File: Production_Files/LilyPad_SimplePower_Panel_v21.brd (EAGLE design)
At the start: 28.4 x 28.4 mm, 20 parts, among them U1 MCP73831

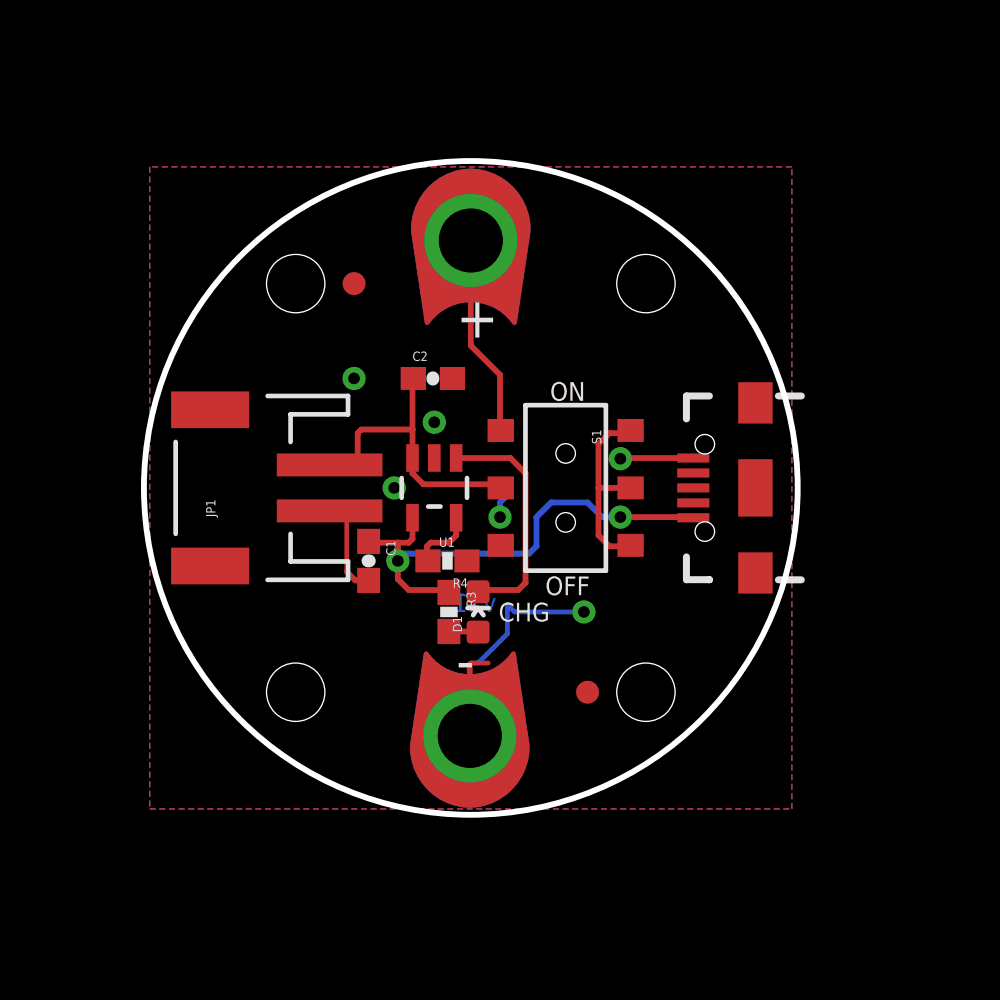
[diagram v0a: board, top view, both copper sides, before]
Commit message: Rotating board 45 degrees for panelization
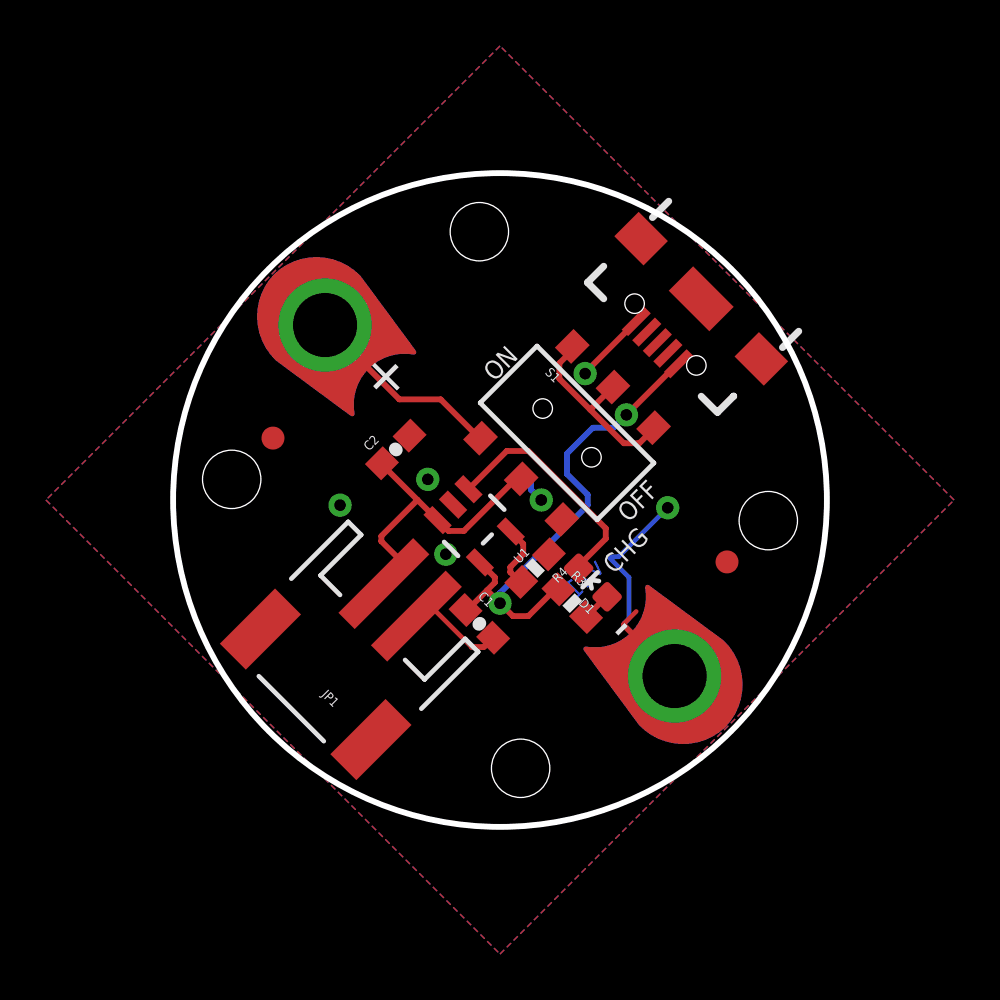
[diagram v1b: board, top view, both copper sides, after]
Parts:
- moved STANDOFF4 10.3 mm to (2.17, -14.7), turned to 45 degrees
- moved JP3 9.31 mm to (8.89, -10.7), turned to 135 degrees
- moved STANDOFF3 9.17 mm to (12.9, -3.96), turned to 45 degrees
- moved STANDOFF1 8.96 mm to (-10.4, -2.17), turned to 45 degrees
- moved JP4 8.56 mm to (10.0, 5.69), turned to 225 degrees
- moved JP1 8.56 mm to (-5.69, -10.0), turned to 135 degrees
- moved FID2 8.30 mm to (11.1, -5.76), turned to 45 degrees
- moved STANDOFF2 7.59 mm to (0.37, 8.61), turned to 45 degrees
- moved FID1 7.59 mm to (-8.61, -0.37), turned to 45 degrees
- moved JP2 7.35 mm to (-6.36, 4.57), turned to 315 degrees
- moved C1 5.54 mm to (0.37, -8.45), turned to 315 degrees
- moved R3 5.38 mm to (4.41, -7.56), turned to 315 degrees
- moved D1 5.15 mm to (5.31, -6.66), turned to 45 degrees
- moved R4 3.83 mm to (2.80, -6.03), turned to 225 degrees
- moved JP5 3.54 mm to (2.39, -5.76), turned to 315 degrees
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
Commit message: Created panel v21
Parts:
- added C10, C11, C12, C13, C14, C15, C16, C17, C18, C19, C20, C21, C22, C23, C24, C25, C26, C27, C28, C29, C3, C30, C31, C32, C33, C34, C35, C36, C37, C38, C39, C4, C40, C41, C42, C43, C44, C45, C46, C47, C48, C49, C5, C50, C51, C52, C53, C54, C55, C56, C57, C58, C59, C6, C60, C61, C62, C63, C64, C7, C8, C9: 4.7uF, SparkFun-Capacitors:0603-CAP
- added D10, D11, D12, D13, D14, D15, D16, D17, D18, D19, D2, D20, D21, D22, D23, D24, D25, D26, D27, D28, D29, D3, D30, D31, D32, D4, D5, D6, D7, D8, D9: Yellow, SparkFun-LED:LED-0603
- added E$1, E$6: (no value), SparkFun-Retired:FIDUCIAL-1.5X3
- added E$2, E$3, E$4, E$5: (no value), SparkFun-Aesthetics:FIDUCIAL-1X2
- added FID10, FID11, FID12, FID13, FID14, FID15, FID16, FID17, FID18, FID19, FID20, FID21, FID22, FID23, FID24, FID25, FID26, FID27, FID28, FID29, FID3, FID30, FID31, FID32, FID33, FID34, FID35, FID36, FID37, FID38, FID39, FID4, FID40, FID41, FID42, FID43, FID44, FID45, FID46, FID47, FID48, FID49, FID5, FID50, FID51, FID52, FID53, FID54, FID55, FID56, FID57, FID58, FID59, FID6, FID60, FID61, FID62, FID63, FID64, FID7, FID8, FID9: FIDUCIAL1X2, SparkFun-Aesthetics:FIDUCIAL-1X2
- added JP10, JP100, JP105, JP110, JP115, JP120, JP125, JP130, JP135, JP140, JP145, JP15, JP150, JP155, JP160, JP20, JP25, JP30, JP35, JP40, JP45, JP50, JP55, JP60, JP65, JP70, JP75, JP80, JP85, JP90, JP95: USB_MICROB_PLUGCONN-11752, SparkFun-Connectors:USB-B-MICRO-SMD_V03
- added JP101, JP106, JP11, JP111, JP116, JP121, JP126, JP131, JP136, JP141, JP146, JP151, JP156, JP16, JP21, JP26, JP31, JP36, JP41, JP46, JP51, JP56, JP6, JP61, JP66, JP71, JP76, JP81, JP86, JP91, JP96: M02-JST-2MM-SMT, SparkFun-Connectors:JST-2-SMD
- added JP102, JP103, JP107, JP108, JP112, JP113, JP117, JP118, JP12, JP122, JP123, JP127, JP128, JP13, JP132, JP133, JP137, JP138, JP142, JP143, JP147, JP148, JP152, JP153, JP157, JP158, JP17, JP18, JP22, JP23, JP27, JP28, JP32, JP33, JP37, JP38, JP42, JP43, JP47, JP48, JP52, JP53, JP57, JP58, JP62, JP63, JP67, JP68, JP7, JP72, JP73, JP77, JP78, JP8, JP82, JP83, JP87, JP88, JP92, JP93, JP97, JP98: SEWTAP9, LilyPad-Wearables:PETAL-LONG-1-2SIDE
- added JP104, JP109, JP114, JP119, JP124, JP129, JP134, JP139, JP14, JP144, JP149, JP154, JP159, JP19, JP24, JP29, JP34, JP39, JP44, JP49, JP54, JP59, JP64, JP69, JP74, JP79, JP84, JP89, JP9, JP94, JP99: SFE_LOGO_FLAME.1_INCH, SparkFun-Aesthetics:SFE_LOGO_FLAME_.1
- added R1, R11, R13, R15, R17, R19, R21, R23, R25, R27, R29, R31, R33, R35, R37, R39, R41, R43, R45, R47, R49, R5, R51, R53, R55, R57, R59, R61, R63, R7, R9: 330, SparkFun-Resistors:0603-RES
- added R10, R12, R14, R16, R18, R2, R20, R22, R24, R26, R28, R30, R32, R34, R36, R38, R40, R42, R44, R46, R48, R50, R52, R54, R56, R58, R6, R60, R62, R64, R8: 2.0k, SparkFun-Resistors:0603-RES
- added S10, S11, S12, S13, S14, S15, S16, S17, S18, S19, S2, S20, S21, S22, S23, S24, S25, S26, S27, S28, S29, S3, S30, S31, S32, S4, S5, S6, S7, S8, S9: DPDT, SparkFun-Electromechanical:AYZ0202
- added STANDOFF10, STANDOFF100, STANDOFF101, STANDOFF102, STANDOFF103, STANDOFF104, STANDOFF105, STANDOFF106, STANDOFF107, STANDOFF108, STANDOFF109, STANDOFF11, STANDOFF110, STANDOFF111, STANDOFF112, STANDOFF113, STANDOFF114, STANDOFF115, STANDOFF116, STANDOFF117, STANDOFF118, STANDOFF119, STANDOFF12, STANDOFF120, STANDOFF121, STANDOFF122, STANDOFF123, STANDOFF124, STANDOFF125, STANDOFF126, STANDOFF127, STANDOFF128, STANDOFF13, STANDOFF14, STANDOFF15, STANDOFF16, STANDOFF17, STANDOFF18, STANDOFF19, STANDOFF20, STANDOFF21, STANDOFF22, STANDOFF23, STANDOFF24, STANDOFF25, STANDOFF26, STANDOFF27, STANDOFF28, STANDOFF29, STANDOFF30, STANDOFF31, STANDOFF32, STANDOFF33, STANDOFF34, STANDOFF35, STANDOFF36, STANDOFF37, STANDOFF38, STANDOFF39, STANDOFF40, STANDOFF41, STANDOFF42, STANDOFF43, STANDOFF44, STANDOFF45, STANDOFF46, STANDOFF47, STANDOFF48, STANDOFF49, STANDOFF5, STANDOFF50, STANDOFF51, STANDOFF52, STANDOFF53, STANDOFF54, STANDOFF55, STANDOFF56, STANDOFF57, STANDOFF58, STANDOFF59, STANDOFF6, STANDOFF60, STANDOFF61, STANDOFF62, STANDOFF63, STANDOFF64, STANDOFF65, STANDOFF66, STANDOFF67, STANDOFF68, STANDOFF69, STANDOFF7, STANDOFF70, STANDOFF71, STANDOFF72, STANDOFF73, STANDOFF74, STANDOFF75, STANDOFF76, STANDOFF77, STANDOFF78, STANDOFF79, STANDOFF8, STANDOFF80, STANDOFF81, STANDOFF82, STANDOFF83, STANDOFF84, STANDOFF85, STANDOFF86, STANDOFF87, STANDOFF88, STANDOFF89, STANDOFF9, STANDOFF90, STANDOFF91, STANDOFF92, STANDOFF93, STANDOFF94, STANDOFF95, STANDOFF96, STANDOFF97, STANDOFF98, STANDOFF99: SEW-HOLE-NO-PAD, Local Library:SEW-HOLE-NO-PAD
- added U$10, U$12, U$14, U$16, U$18, U$20, U$22, U$24, U$26, U$28, U$3, U$30, U$32, U$34, U$36, U$38, U$40, U$42, U$44, U$46, U$48, U$50, U$52, U$54, U$56, U$58, U$6, U$60, U$62, U$64, U$8: LOGO-LPLP, LilyPad-Wearables:LOGO-LILYPAD
- added U$11, U$13, U$15, U$17, U$19, U$2, U$21, U$23, U$25, U$27, U$29, U$31, U$33, U$35, U$37, U$39, U$4, U$41, U$43, U$45, U$47, U$49, U$51, U$53, U$55, U$57, U$59, U$61, U$63, U$7, U$9: OSHW-LOGOS, SparkFun-Aesthetics:OSHW-LOGO-S
- added U10, U11, U12, U13, U14, U15, U16, U17, U18, U19, U2, U20, U21, U22, U23, U24, U25, U26, U27, U28, U29, U3, U30, U31, U32, U4, U5, U6, U7, U8, U9: MCP73831, SparkFun-PowerIC:SOT23-5
- moved FID2 35.1 mm to (34.0, 20.9)
- moved C1 35.1 mm to (23.2, 18.2)
- moved C2 35.1 mm to (19.6, 25.8)
- moved D1 35.1 mm to (28.2, 20.0)
- moved FID1 35.1 mm to (14.3, 26.3)
- moved JP1 35.1 mm to (17.2, 16.6)
- moved JP2 35.1 mm to (16.5, 31.2)
- moved JP3 35.1 mm to (31.7, 15.9)
- moved JP4 35.1 mm to (32.9, 32.4)
- moved JP5 35.1 mm to (25.3, 20.9)
- moved R3 35.1 mm to (27.3, 19.1)
- moved R4 35.1 mm to (25.7, 20.6)
- moved S1 35.1 mm to (27.0, 26.5)
- moved STANDOFF1 35.1 mm to (12.5, 24.5)
- moved STANDOFF2 35.1 mm to (23.2, 35.3)
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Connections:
- new net GND1: C3.2, C4.2, JP10.GND1, JP6.1, JP7.1, R2.1, U2.2
- new net GND10: C21.2, C22.2, JP51.1, JP52.1, JP55.GND1, R22.1, U11.2
- new net GND11: C23.2, C24.2, JP56.1, JP57.1, JP60.GND1, R24.1, U12.2
- new net GND12: C25.2, C26.2, JP61.1, JP62.1, JP65.GND1, R26.1, U13.2
- new net GND13: C27.2, C28.2, JP66.1, JP67.1, JP70.GND1, R28.1, U14.2
- new net GND14: C29.2, C30.2, JP71.1, JP72.1, JP75.GND1, R30.1, U15.2
- new net GND15: C31.2, C32.2, JP76.1, JP77.1, JP80.GND1, R32.1, U16.2
- new net GND16: C33.2, C34.2, JP81.1, JP82.1, JP85.GND1, R34.1, U17.2
- new net GND17: C35.2, C36.2, JP86.1, JP87.1, JP90.GND1, R36.1, U18.2
- new net GND18: C37.2, C38.2, JP91.1, JP92.1, JP95.GND1, R38.1, U19.2
- new net GND19: C39.2, C40.2, JP100.GND1, JP96.1, JP97.1, R40.1, U20.2
- new net GND2: C5.2, C6.2, JP11.1, JP12.1, JP15.GND1, R6.1, U3.2
- new net GND20: C41.2, C42.2, JP101.1, JP102.1, JP105.GND1, R42.1, U21.2
- new net GND21: C43.2, C44.2, JP106.1, JP107.1, JP110.GND1, R44.1, U22.2
- new net GND22: C45.2, C46.2, JP111.1, JP112.1, JP115.GND1, R46.1, U23.2
- new net GND23: C47.2, C48.2, JP116.1, JP117.1, JP120.GND1, R48.1, U24.2
- new net GND24: C49.2, C50.2, JP121.1, JP122.1, JP125.GND1, R50.1, U25.2
- new net GND25: C51.2, C52.2, JP126.1, JP127.1, JP130.GND1, R52.1, U26.2
- new net GND26: C53.2, C54.2, JP131.1, JP132.1, JP135.GND1, R54.1, U27.2
- new net GND27: C55.2, C56.2, JP136.1, JP137.1, JP140.GND1, R56.1, U28.2
- new net GND28: C57.2, C58.2, JP141.1, JP142.1, JP145.GND1, R58.1, U29.2
- new net GND29: C59.2, C60.2, JP146.1, JP147.1, JP150.GND1, R60.1, U30.2
- new net GND3: C7.2, C8.2, JP16.1, JP17.1, JP20.GND1, R8.1, U4.2
- new net GND30: C61.2, C62.2, JP151.1, JP152.1, JP155.GND1, R62.1, U31.2
- new net GND31: C63.2, C64.2, JP156.1, JP157.1, JP160.GND1, R64.1, U32.2
- new net GND4: C10.2, C9.2, JP21.1, JP22.1, JP25.GND1, R10.1, U5.2
- new net GND5: C11.2, C12.2, JP26.1, JP27.1, JP30.GND1, R12.1, U6.2
- new net GND6: C13.2, C14.2, JP31.1, JP32.1, JP35.GND1, R14.1, U7.2
- new net GND7: C15.2, C16.2, JP36.1, JP37.1, JP40.GND1, R16.1, U8.2
- new net GND8: C17.2, C18.2, JP41.1, JP42.1, JP45.GND1, R18.1, U9.2
- new net GND9: C19.2, C20.2, JP46.1, JP47.1, JP50.GND1, R20.1, U10.2
- new net N$10: R2.2, U2.5
- new net N$100: R40.2, U20.5
- new net N$101: C42.1, JP101.2, S21.5, U21.3
- new net N$102: C41.1, JP105.VBUS1, R41.1, U21.4
- new net N$103: D21.C, U21.1
- new net N$104: D21.A, R41.2
- new net N$105: R42.2, U21.5
- new net N$106: C44.1, JP106.2, S22.5, U22.3
- new net N$107: C43.1, JP110.VBUS1, R43.1, U22.4
- new net N$108: D22.C, U22.1
- new net N$109: D22.A, R43.2
- new net N$11: C6.1, JP11.2, S3.5, U3.3
- new net N$110: R44.2, U22.5
- new net N$111: C46.1, JP111.2, S23.5, U23.3
- new net N$112: C45.1, JP115.VBUS1, R45.1, U23.4
- new net N$113: D23.C, U23.1
- new net N$114: D23.A, R45.2
- new net N$115: R46.2, U23.5
- new net N$116: C48.1, JP116.2, S24.5, U24.3
- new net N$117: C47.1, JP120.VBUS1, R47.1, U24.4
- new net N$118: D24.C, U24.1
- new net N$119: D24.A, R47.2
- new net N$12: C5.1, JP15.VBUS1, R5.1, U3.4
- new net N$120: R48.2, U24.5
- new net N$121: C50.1, JP121.2, S25.5, U25.3
- new net N$122: C49.1, JP125.VBUS1, R49.1, U25.4
- new net N$123: D25.C, U25.1
- new net N$124: D25.A, R49.2
- new net N$125: R50.2, U25.5
- new net N$126: C52.1, JP126.2, S26.5, U26.3
- new net N$127: C51.1, JP130.VBUS1, R51.1, U26.4
- new net N$128: D26.C, U26.1
- new net N$129: D26.A, R51.2
- new net N$13: D3.C, U3.1
- new net N$130: R52.2, U26.5
- new net N$131: C54.1, JP131.2, S27.5, U27.3
- new net N$132: C53.1, JP135.VBUS1, R53.1, U27.4
- new net N$133: D27.C, U27.1
- new net N$134: D27.A, R53.2
- new net N$135: R54.2, U27.5
- new net N$136: C56.1, JP136.2, S28.5, U28.3
- new net N$137: C55.1, JP140.VBUS1, R55.1, U28.4
- new net N$138: D28.C, U28.1
- new net N$139: D28.A, R55.2
- new net N$14: D3.A, R5.2
- new net N$140: R56.2, U28.5
- new net N$141: C58.1, JP141.2, S29.5, U29.3
- new net N$142: C57.1, JP145.VBUS1, R57.1, U29.4
- new net N$143: D29.C, U29.1
- new net N$144: D29.A, R57.2
- new net N$145: R58.2, U29.5
- new net N$146: C60.1, JP146.2, S30.5, U30.3
- new net N$147: C59.1, JP150.VBUS1, R59.1, U30.4
- new net N$148: D30.C, U30.1
- new net N$149: D30.A, R59.2
- new net N$15: R6.2, U3.5
- new net N$150: R60.2, U30.5
- new net N$151: C62.1, JP151.2, S31.5, U31.3
- new net N$152: C61.1, JP155.VBUS1, R61.1, U31.4
- new net N$153: D31.C, U31.1
- new net N$154: D31.A, R61.2
- new net N$155: R62.2, U31.5
- new net N$156: C64.1, JP156.2, S32.5, U32.3
- new net N$157: C63.1, JP160.VBUS1, R63.1, U32.4
- new net N$158: D32.C, U32.1
- new net N$159: D32.A, R63.2
- new net N$16: C8.1, JP16.2, S4.5, U4.3
- new net N$160: R64.2, U32.5
- new net N$17: C7.1, JP20.VBUS1, R7.1, U4.4
- new net N$18: D4.C, U4.1
- new net N$19: D4.A, R7.2
- new net N$2: C4.1, JP6.2, S2.5, U2.3
- new net N$20: R8.2, U4.5
- new net N$21: C10.1, JP21.2, S5.5, U5.3
- new net N$22: C9.1, JP25.VBUS1, R9.1, U5.4
- new net N$23: D5.C, U5.1
- new net N$24: D5.A, R9.2
- new net N$25: R10.2, U5.5
- new net N$26: C12.1, JP26.2, S6.5, U6.3
- new net N$27: C11.1, JP30.VBUS1, R11.1, U6.4
- new net N$28: D6.C, U6.1
- new net N$29: D6.A, R11.2
- new net N$30: R12.2, U6.5
- new net N$31: C14.1, JP31.2, S7.5, U7.3
- new net N$32: C13.1, JP35.VBUS1, R13.1, U7.4
- new net N$33: D7.C, U7.1
- new net N$34: D7.A, R13.2
- new net N$35: R14.2, U7.5
- new net N$36: C16.1, JP36.2, S8.5, U8.3
- new net N$37: C15.1, JP40.VBUS1, R15.1, U8.4
- new net N$38: D8.C, U8.1
- new net N$39: D8.A, R15.2
- new net N$40: R16.2, U8.5
- new net N$41: C18.1, JP41.2, S9.5, U9.3
- new net N$42: C17.1, JP45.VBUS1, R17.1, U9.4
- new net N$43: D9.C, U9.1
- new net N$44: D9.A, R17.2
- new net N$45: R18.2, U9.5
- new net N$46: C20.1, JP46.2, S10.5, U10.3
- new net N$47: C19.1, JP50.VBUS1, R19.1, U10.4
- new net N$48: D10.C, U10.1
- new net N$49: D10.A, R19.2
- new net N$50: R20.2, U10.5
- new net N$51: C22.1, JP51.2, S11.5, U11.3
- new net N$52: C21.1, JP55.VBUS1, R21.1, U11.4
- new net N$53: D11.C, U11.1
- new net N$54: D11.A, R21.2
- new net N$55: R22.2, U11.5
- new net N$56: C24.1, JP56.2, S12.5, U12.3
- new net N$57: C23.1, JP60.VBUS1, R23.1, U12.4
- new net N$58: D12.C, U12.1
- new net N$59: D12.A, R23.2
- new net N$6: C3.1, JP10.VBUS1, R1.1, U2.4
- new net N$60: R24.2, U12.5
- new net N$61: C26.1, JP61.2, S13.5, U13.3
- new net N$62: C25.1, JP65.VBUS1, R25.1, U13.4
- new net N$63: D13.C, U13.1
- new net N$64: D13.A, R25.2
- new net N$65: R26.2, U13.5
- new net N$66: C28.1, JP66.2, S14.5, U14.3
- new net N$67: C27.1, JP70.VBUS1, R27.1, U14.4
- new net N$68: D14.C, U14.1
- new net N$69: D14.A, R27.2
- new net N$70: R28.2, U14.5
- new net N$71: C30.1, JP71.2, S15.5, U15.3
- new net N$72: C29.1, JP75.VBUS1, R29.1, U15.4
- new net N$73: D15.C, U15.1
- new net N$74: D15.A, R29.2
- new net N$75: R30.2, U15.5
- new net N$76: C32.1, JP76.2, S16.5, U16.3
- new net N$77: C31.1, JP80.VBUS1, R31.1, U16.4
- new net N$78: D16.C, U16.1
- new net N$79: D16.A, R31.2
- new net N$8: D2.C, U2.1
- new net N$80: R32.2, U16.5
- new net N$81: C34.1, JP81.2, S17.5, U17.3
- new net N$82: C33.1, JP85.VBUS1, R33.1, U17.4
- new net N$83: D17.C, U17.1
- new net N$84: D17.A, R33.2
- new net N$85: R34.2, U17.5
- new net N$86: C36.1, JP86.2, S18.5, U18.3
- new net N$87: C35.1, JP90.VBUS1, R35.1, U18.4
- new net N$88: D18.C, U18.1
- new net N$89: D18.A, R35.2
- new net N$9: D2.A, R1.2
- new net N$90: R36.2, U18.5
- new net N$91: C38.1, JP91.2, S19.5, U19.3
- new net N$92: C37.1, JP95.VBUS1, R37.1, U19.4
- new net N$93: D19.C, U19.1
- new net N$94: D19.A, R37.2
- new net N$95: R38.2, U19.5
- new net N$96: C40.1, JP96.2, S20.5, U20.3
- new net N$97: C39.1, JP100.VBUS1, R39.1, U20.4
- new net N$98: D20.C, U20.1
- new net N$99: D20.A, R39.2
- new net SINK10: S10.1, S10.2, S10.3
- new net SINK11: S11.1, S11.2, S11.3
- new net SINK12: S12.1, S12.2, S12.3
- new net SINK13: S13.1, S13.2, S13.3
- new net SINK14: S14.1, S14.2, S14.3
- new net SINK15: S15.1, S15.2, S15.3
- new net SINK16: S16.1, S16.2, S16.3
- new net SINK17: S17.1, S17.2, S17.3
- new net SINK18: S18.1, S18.2, S18.3
- new net SINK19: S19.1, S19.2, S19.3
- new net SINK2: S2.1, S2.2, S2.3
- new net SINK20: S20.1, S20.2, S20.3
- new net SINK21: S21.1, S21.2, S21.3
- new net SINK22: S22.1, S22.2, S22.3
- new net SINK23: S23.1, S23.2, S23.3
- new net SINK24: S24.1, S24.2, S24.3
- new net SINK25: S25.1, S25.2, S25.3
- new net SINK26: S26.1, S26.2, S26.3
- new net SINK27: S27.1, S27.2, S27.3
- new net SINK28: S28.1, S28.2, S28.3
- new net SINK29: S29.1, S29.2, S29.3
- new net SINK3: S3.1, S3.2, S3.3
- new net SINK30: S30.1, S30.2, S30.3
- new net SINK31: S31.1, S31.2, S31.3
- new net SINK32: S32.1, S32.2, S32.3
- new net SINK4: S4.1, S4.2, S4.3
- new net SINK5: S5.1, S5.2, S5.3
- new net SINK6: S6.1, S6.2, S6.3
- new net SINK7: S7.1, S7.2, S7.3
- new net SINK8: S8.1, S8.2, S8.3
- new net SINK9: S9.1, S9.2, S9.3
- new net VCC1: JP8.1, S2.4
- new net VCC10: JP53.1, S11.4
- new net VCC11: JP58.1, S12.4
- new net VCC12: JP63.1, S13.4
- new net VCC13: JP68.1, S14.4
- new net VCC14: JP73.1, S15.4
- new net VCC15: JP78.1, S16.4
- new net VCC16: JP83.1, S17.4
- new net VCC17: JP88.1, S18.4
- new net VCC18: JP93.1, S19.4
- new net VCC19: JP98.1, S20.4
- new net VCC2: JP13.1, S3.4
- new net VCC20: JP103.1, S21.4
- new net VCC21: JP108.1, S22.4
- new net VCC22: JP113.1, S23.4
- new net VCC23: JP118.1, S24.4
- new net VCC24: JP123.1, S25.4
- new net VCC25: JP128.1, S26.4
- new net VCC26: JP133.1, S27.4
- new net VCC27: JP138.1, S28.4
- new net VCC28: JP143.1, S29.4
- new net VCC29: JP148.1, S30.4
- new net VCC3: JP18.1, S4.4
- new net VCC30: JP153.1, S31.4
- new net VCC31: JP158.1, S32.4
- new net VCC4: JP23.1, S5.4
- new net VCC5: JP28.1, S6.4
- new net VCC6: JP33.1, S7.4
- new net VCC7: JP38.1, S8.4
- new net VCC8: JP43.1, S9.4
- new net VCC9: JP48.1, S10.4
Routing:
- net N$37: track 0.00 -> 21.9 mm, vias 0 -> 2
- net N$32: track 0.00 -> 21.9 mm, vias 0 -> 2
- net N$27: track 0.00 -> 21.9 mm, vias 0 -> 2
- net N$6: track 0.00 -> 21.9 mm, vias 0 -> 2
- net N$17: track 0.00 -> 21.9 mm, vias 0 -> 2
- net N$12: track 0.00 -> 21.9 mm, vias 0 -> 2
- net N$67: track 0.00 -> 21.9 mm, vias 0 -> 2
- net N$47: track 0.00 -> 21.9 mm, vias 0 -> 2
- net N$77: track 0.00 -> 21.9 mm, vias 0 -> 2
- net N$72: track 0.00 -> 21.9 mm, vias 0 -> 2
- net N$57: track 0.00 -> 21.9 mm, vias 0 -> 2
- net N$52: track 0.00 -> 21.9 mm, vias 0 -> 2
- net N$22: track 0.00 -> 21.9 mm, vias 0 -> 2
- net N$62: track 0.00 -> 21.9 mm, vias 0 -> 2
- net N$42: track 0.00 -> 21.9 mm, vias 0 -> 2
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- added copper zone on layer 1, net GND1
- added copper zone on layer 16, net GND1
- added copper zone on layer 1, net GND10
- added copper zone on layer 16, net GND10
- added copper zone on layer 1, net GND11
- added copper zone on layer 16, net GND11
- added copper zone on layer 1, net GND12
- added copper zone on layer 16, net GND12
- added copper zone on layer 1, net GND13
- added copper zone on layer 16, net GND13
- added copper zone on layer 1, net GND14
- added copper zone on layer 16, net GND14
- added copper zone on layer 1, net GND15
- added copper zone on layer 16, net GND15
- added copper zone on layer 1, net GND16
- added copper zone on layer 16, net GND16
- added copper zone on layer 1, net GND17
- added copper zone on layer 16, net GND17
- added copper zone on layer 1, net GND18
- added copper zone on layer 16, net GND18
- added copper zone on layer 1, net GND19
- added copper zone on layer 16, net GND19
- added copper zone on layer 1, net GND2
- added copper zone on layer 16, net GND2
- added copper zone on layer 1, net GND20
- added copper zone on layer 16, net GND20
- added copper zone on layer 1, net GND21
- added copper zone on layer 16, net GND21
- added copper zone on layer 1, net GND22
- added copper zone on layer 16, net GND22
- added copper zone on layer 1, net GND23
- added copper zone on layer 16, net GND23
- added copper zone on layer 1, net GND24
- added copper zone on layer 16, net GND24
- added copper zone on layer 1, net GND25
- added copper zone on layer 16, net GND25
- added copper zone on layer 1, net GND26
- added copper zone on layer 16, net GND26
- added copper zone on layer 1, net GND27
- added copper zone on layer 16, net GND27
- added copper zone on layer 1, net GND28
- added copper zone on layer 16, net GND28
- added copper zone on layer 1, net GND29
- added copper zone on layer 16, net GND29
- added copper zone on layer 1, net GND3
- added copper zone on layer 16, net GND3
- added copper zone on layer 1, net GND30
- added copper zone on layer 16, net GND30
- added copper zone on layer 1, net GND31
- added copper zone on layer 16, net GND31
- added copper zone on layer 1, net GND4
- added copper zone on layer 16, net GND4
- added copper zone on layer 1, net GND5
- added copper zone on layer 16, net GND5
- added copper zone on layer 1, net GND6
- added copper zone on layer 16, net GND6
- added copper zone on layer 1, net GND7
- added copper zone on layer 16, net GND7
- added copper zone on layer 1, net GND8
- added copper zone on layer 16, net GND8
- added copper zone on layer 1, net GND9
- added copper zone on layer 16, net GND9
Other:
- board size 28.4 x 28.4 mm -> 287.5 x 142.2 mm
